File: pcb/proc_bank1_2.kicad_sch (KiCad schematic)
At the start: 3 parts, among them U1 XC6SLX9-TQG144, U14 ECS-7050MV

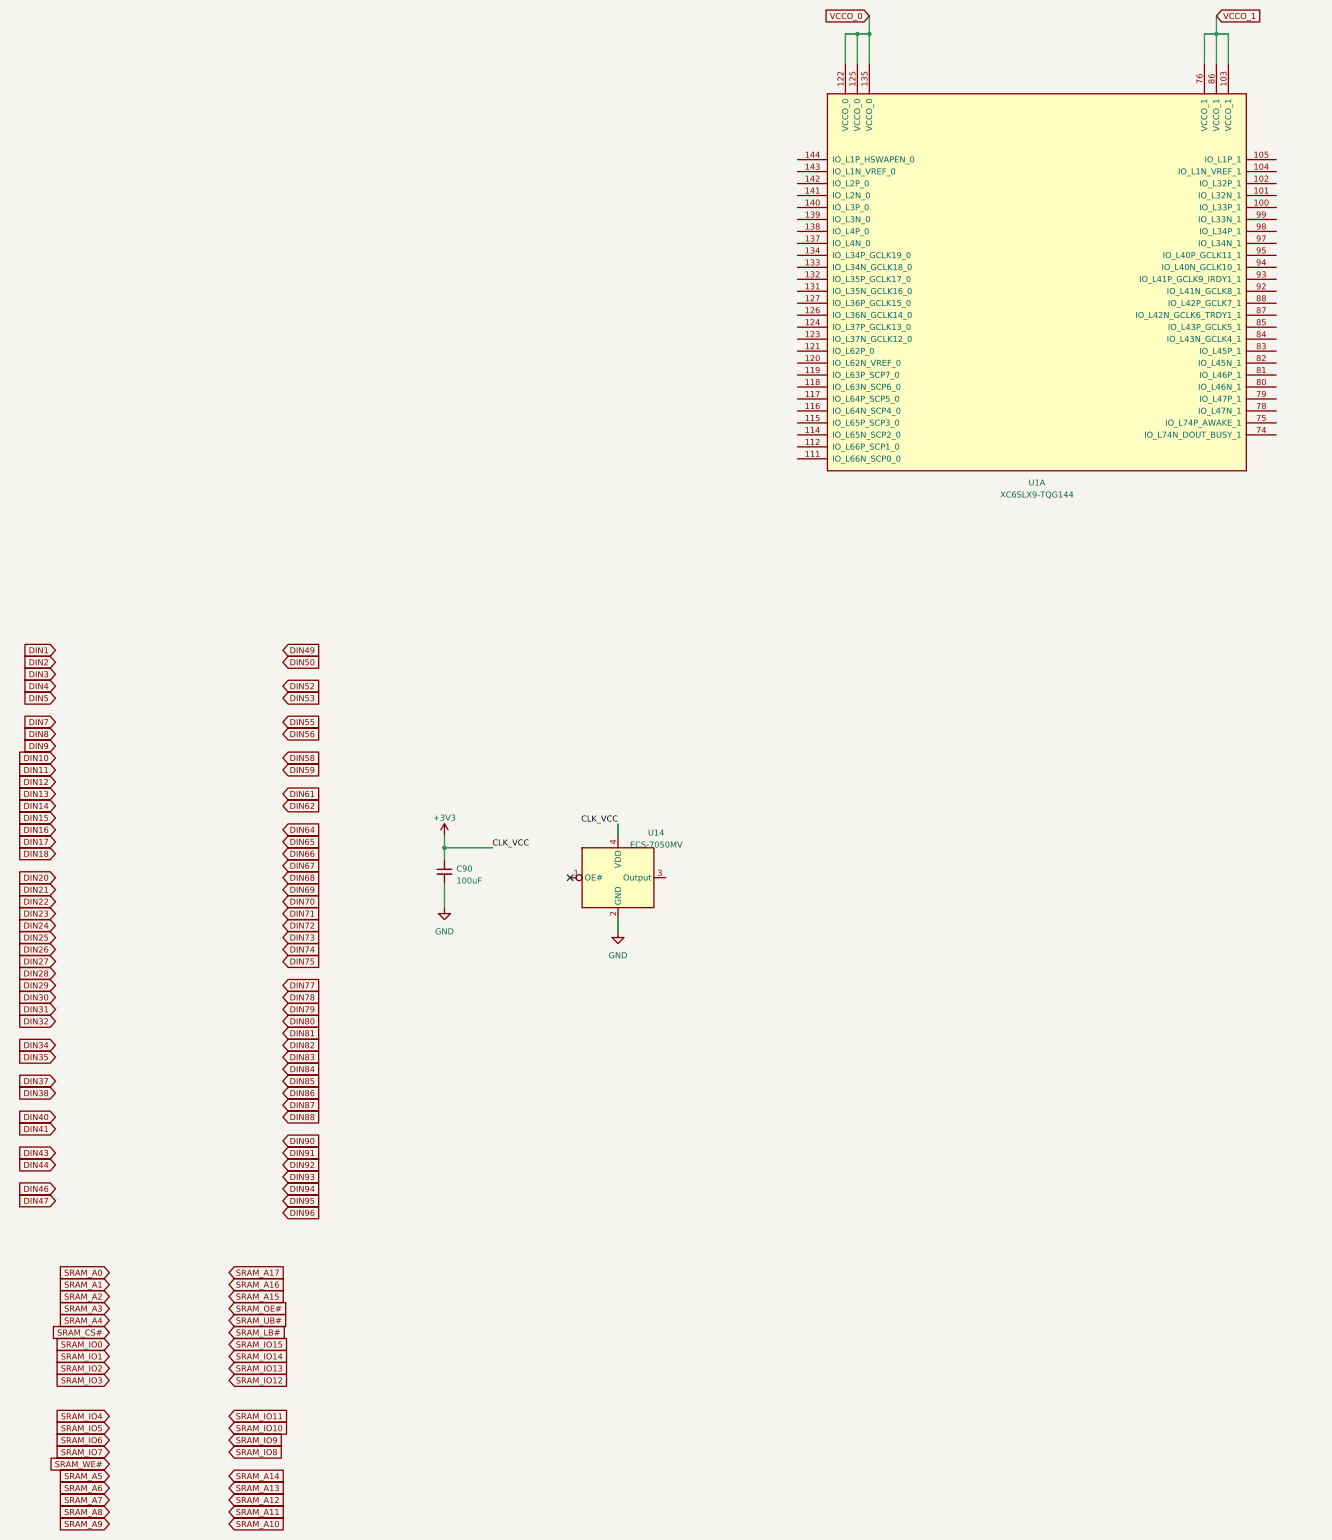
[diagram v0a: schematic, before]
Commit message: added silkscreen values
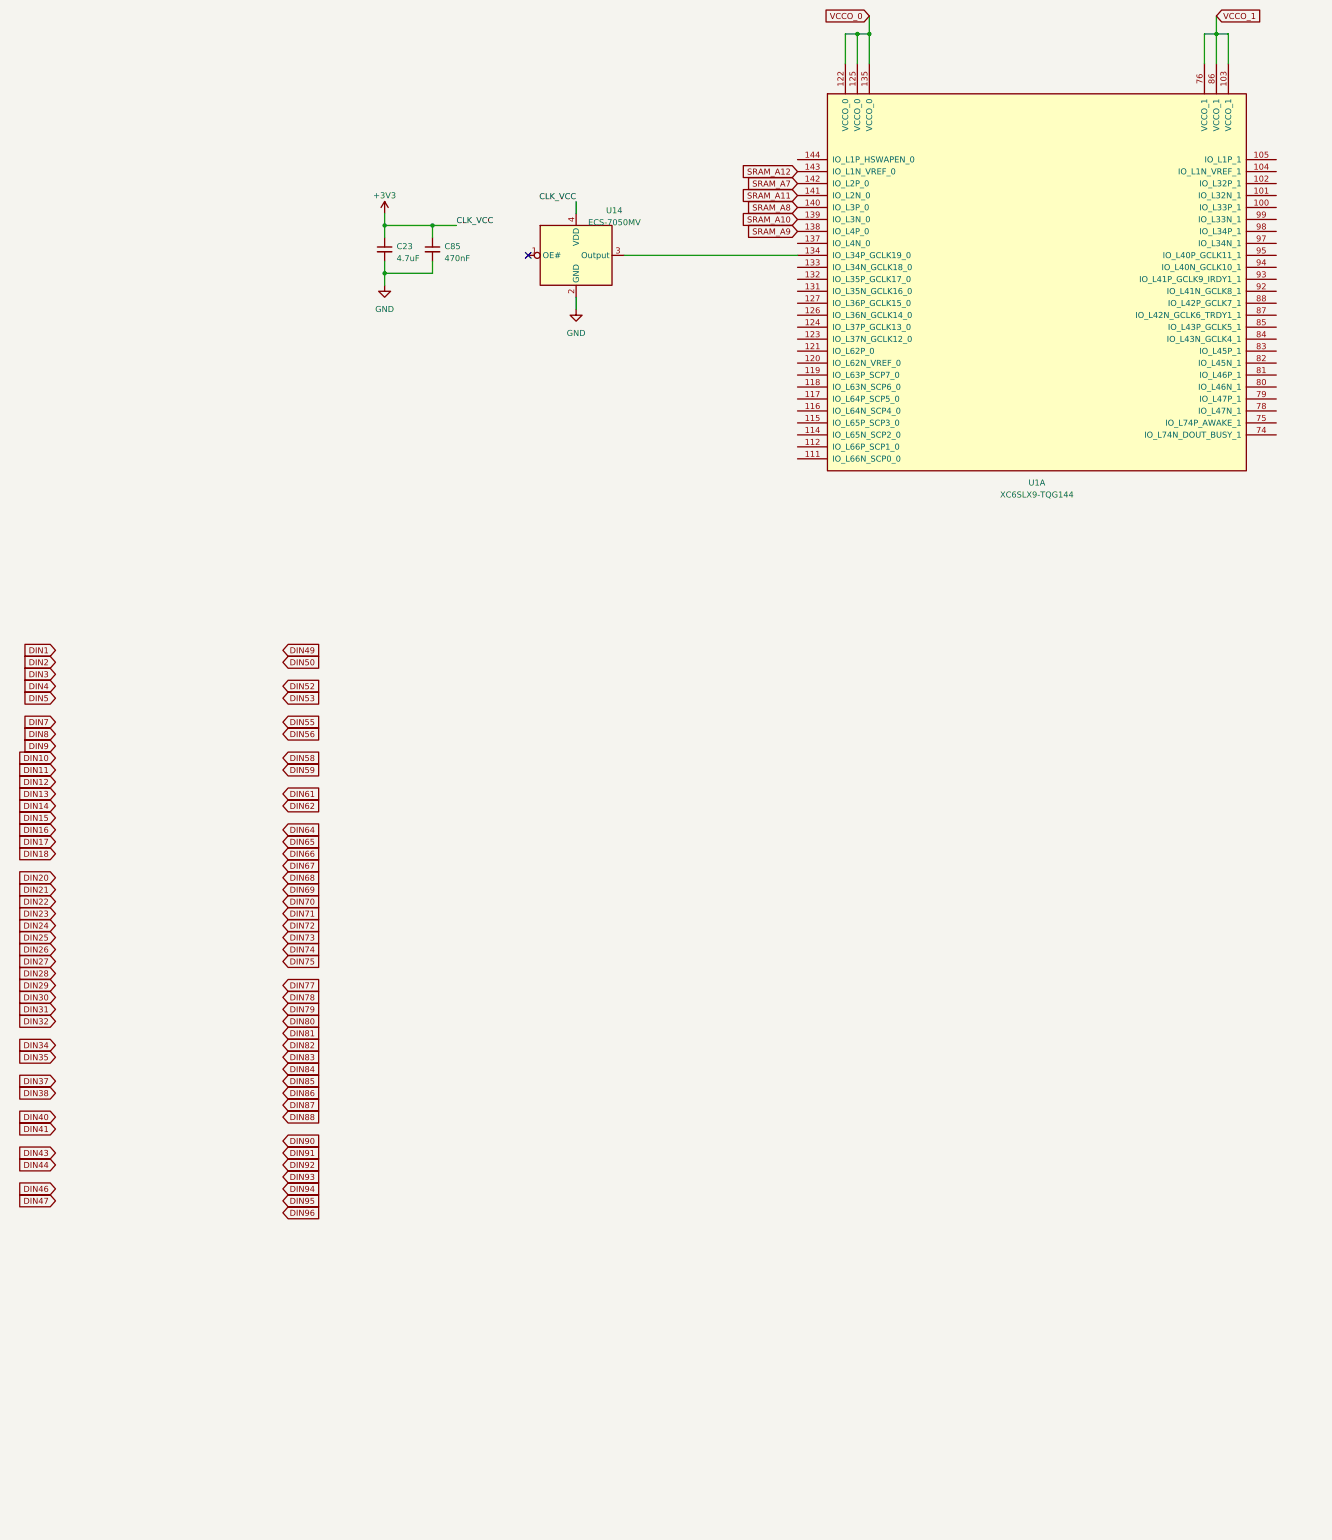
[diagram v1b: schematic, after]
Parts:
- removed C90: 100uF, Capacitor_SMD:C_1210_3225Metric, symbol Device:C_Small
- added C23: 4.7uF, Capacitor_SMD:C_0805_2012Metric, symbol Device:C_Small
- added C85: 470nF, Capacitor_SMD:C_0402_1005Metric, symbol Device:C_Small
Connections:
- net +3V3: now also C23.1, C85.1
- net GND: now also C23.2, C85.2
- net SRAM_A10: now also U1.139 (IO_L3N_0)
- net SRAM_A11: now also U1.141 (IO_L2N_0)
- net SRAM_A12: now also U1.143 (IO_L1N_VREF_0)
- net SRAM_A7: now also U1.142 (IO_L2P_0)
- net SRAM_A8: now also U1.140 (IO_L3P_0)
- net SRAM_A9: now also U1.138 (IO_L4P_0)
- net at U1.134 (IO_L34P_GCLK19_0): now also U14.3 (Output)
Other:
- moved on the sheet: U14

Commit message: edit the connector pinout
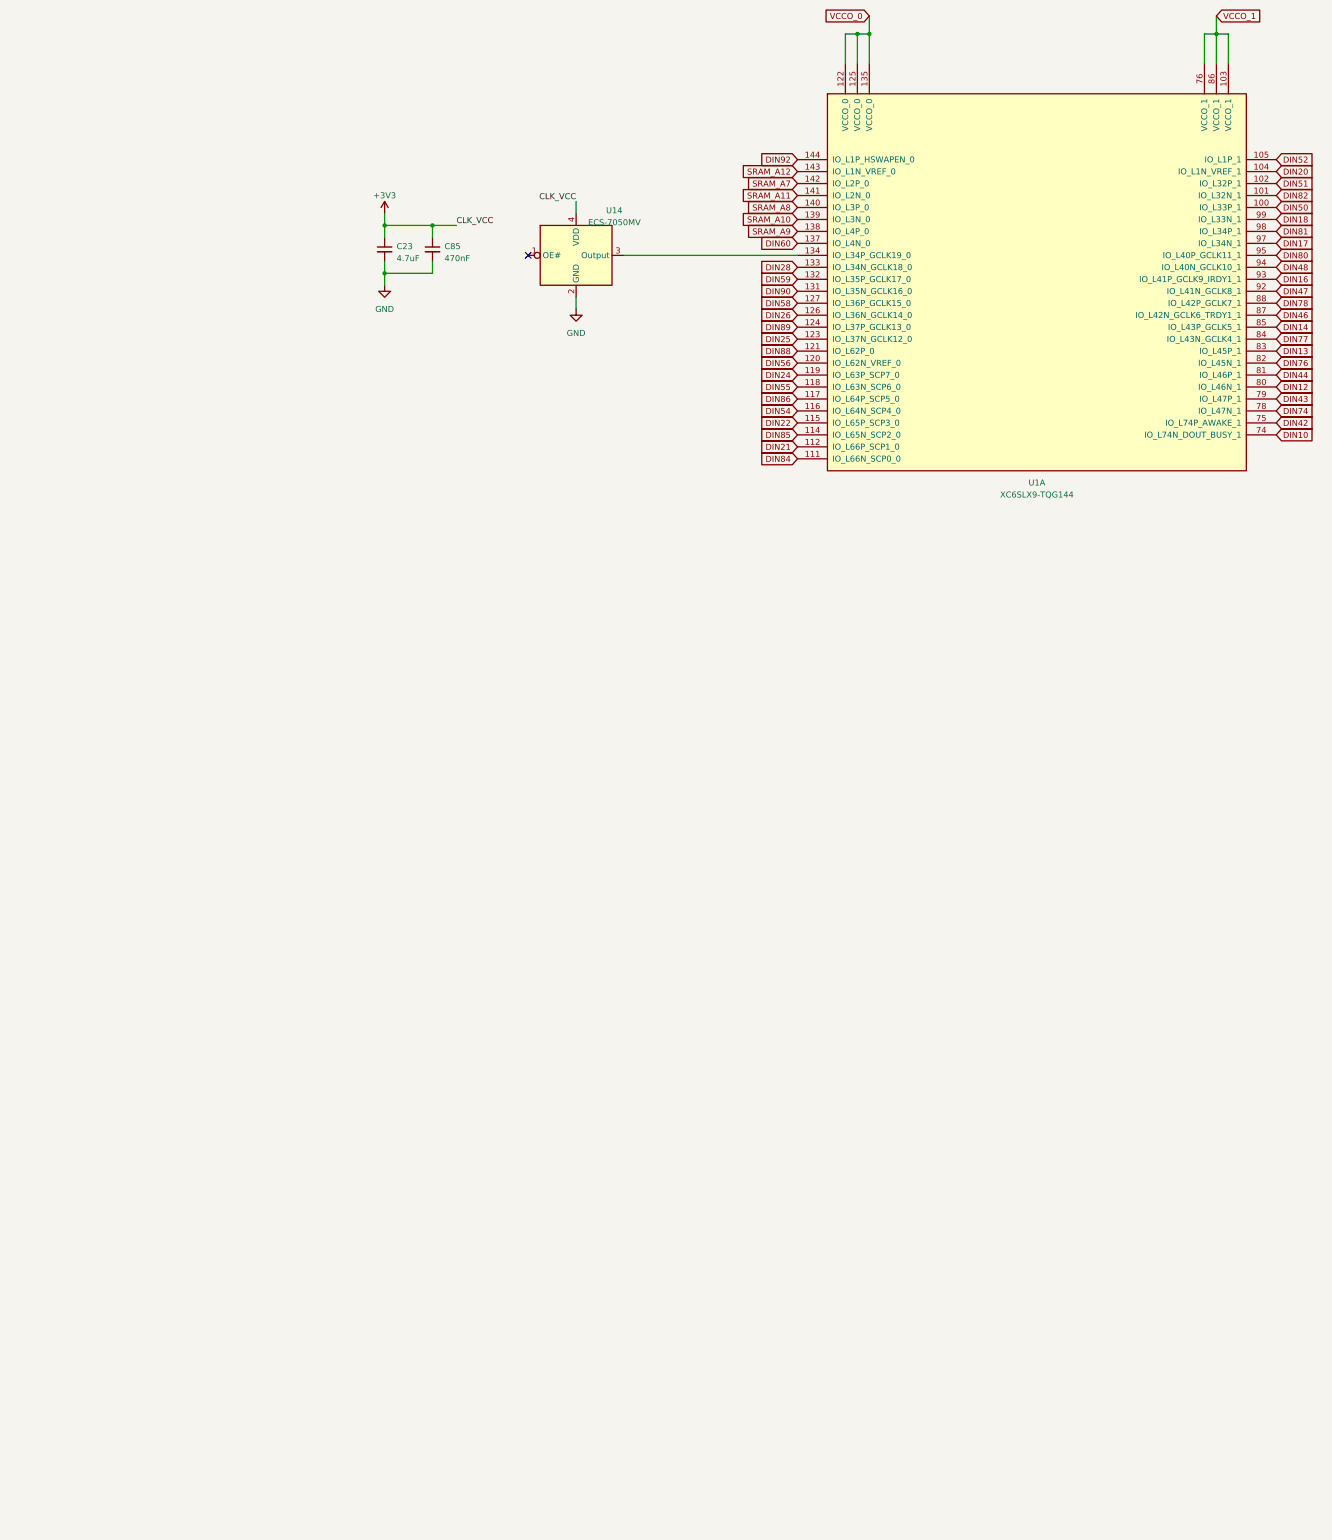
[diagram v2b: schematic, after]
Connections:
- net DIN10: now also U1.74 (IO_L74N_DOUT_BUSY_1)
- net DIN12: now also U1.80 (IO_L46N_1)
- net DIN13: now also U1.83 (IO_L45P_1)
- net DIN14: now also U1.85 (IO_L43P_GCLK5_1)
- net DIN16: now also U1.93 (IO_L41P_GCLK9_IRDY1_1)
- net DIN17: now also U1.97 (IO_L34N_1)
- net DIN18: now also U1.99 (IO_L33N_1)
- net DIN20: now also U1.104 (IO_L1N_VREF_1)
- net DIN21: now also U1.112 (IO_L66P_SCP1_0)
- net DIN22: now also U1.115 (IO_L65P_SCP3_0)
- net DIN24: now also U1.119 (IO_L63P_SCP7_0)
- net DIN25: now also U1.123 (IO_L37N_GCLK12_0)
- net DIN26: now also U1.126 (IO_L36N_GCLK14_0)
- net DIN28: now also U1.133 (IO_L34N_GCLK18_0)
- net DIN43: now also U1.79 (IO_L47P_1)
- net DIN44: now also U1.81 (IO_L46P_1)
- net DIN46: now also U1.87 (IO_L42N_GCLK6_TRDY1_1)
- net DIN47: now also U1.92 (IO_L41N_GCLK8_1)
- net DIN50: now also U1.100 (IO_L33P_1)
- net DIN52: now also U1.105 (IO_L1P_1)
- net DIN55: now also U1.118 (IO_L63N_SCP6_0)
- net DIN56: now also U1.120 (IO_L62N_VREF_0)
- net DIN58: now also U1.127 (IO_L36P_GCLK15_0)
- net DIN59: now also U1.132 (IO_L35P_GCLK17_0)
- net DIN74: now also U1.78 (IO_L47N_1)
- net DIN77: now also U1.84 (IO_L43N_GCLK4_1)
- net DIN78: now also U1.88 (IO_L42P_GCLK7_1)
- net DIN80: now also U1.95 (IO_L40P_GCLK11_1)
- net DIN81: now also U1.98 (IO_L34P_1)
- net DIN82: now also U1.101 (IO_L32N_1)
- net DIN84: now also U1.111 (IO_L66N_SCP0_0)
- net DIN85: now also U1.114 (IO_L65N_SCP2_0)
- net DIN86: now also U1.117 (IO_L64P_SCP5_0)
- net DIN88: now also U1.121 (IO_L62P_0)
- net DIN90: now also U1.131 (IO_L35N_GCLK16_0)
- net DIN92: now also U1.144 (IO_L1P_HSWAPEN_0)
- net DIN51: now reaches U1.102 (IO_L32P_1)
- net DIN54: now reaches U1.116 (IO_L64N_SCP4_0)
- net DIN89: now reaches U1.124 (IO_L37P_GCLK13_0)
- net DIN60: now reaches U1.137 (IO_L4N_0)
- net DIN42: now reaches U1.75 (IO_L74P_AWAKE_1)
- net DIN76: now reaches U1.82 (IO_L45N_1)
- net DIN48: now reaches U1.94 (IO_L40N_GCLK10_1)
